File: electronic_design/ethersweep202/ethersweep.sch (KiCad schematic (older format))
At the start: 72 parts, among them J1 AVR-ISP-6, J2 Conn_01x02_Male, J3 Conn_01x04_Female, J4 Conn_01x02_Male, J5 Conn_01x02_Male, J6 HR911105A, J7 Conn_01x06_Female, J8 AVR-ISP-6, J9 Conn_01x06_Male, M1 Stepper_Motor_bipolar, SW1 SW_Push, U1 ENC28J60x-SS, U2 ATmega328-AU, U3 DRV8825PWPR, U4 AMS1117-3.3, U5 AS5600, Y1 Crystal_25MHz, Y3 Crystal

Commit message: minor v202 changes
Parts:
- added C?: C10uF, Capacitor_SMD:C_0805_2012Metric, symbol Device:C
- added C? (x6): C100nF, Capacitor_SMD:C_0805_2012Metric, symbol Device:C
- added C? (x2): C1uF, Capacitor_SMD:C_0805_2012Metric, symbol Device:C
- added J?: HR911105A, modules:HANRUN_HR911105A, symbol HR911105A:HR911105A
- added R?: R2M, symbol Device:R
- added R? (x2): R330, Resistor_SMD:R_0603_1608Metric, symbol Device:R
- added U?: W5500, Package_QFP:LQFP-48_7x7mm_P0.5mm, symbol Interface_Ethernet:W5500
- C4, C5: value C22pF -> C18pF
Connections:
- net +3V3: now also C?.1, C?.1, C?.1, C?.1, C?.1, C?.1, C?.1, C?.1, C?.1, J?.4, J?.5, U?.11 (AVDD), U?.15 (AVDD), U?.17 (AVDD), U?.21 (AVDD), U?.28 (VDD), U?.4 (AVDD), U?.8 (AVDD)
- net CS_ETHERNET: now also U?.32 (~SCS)
- net ENC_RD+: now also J?.3
- net ENC_RD-: now also J?.6
- net ENC_TD+: now also J?.1
- net ENC_TD-: now also J?.2
- net ETHERNET_LED_A: now also J?.12, R?.1
- net ETHERNET_LED_B: now also J?.9, R?.1
- net GND: now also C?.2, C?.2, C?.2, C?.2, C?.2, C?.2, C?.2, C?.2, C?.2, J?.10, J?.11, J?.15 (SHIELD), J?.16 (SHIELD), J?.8
- net MISO: now also U?.34 (MISO)
- net MOSI: now also U?.35 (MOSI)
- net SCK: now also U?.33 (SCLK)
- net at C4.2, U1.23 (OSC1), Y1.3: now also R?.1
- net at C5.1, U1.24 (OSC2), Y1.1: now also R?.2
- new net: U?.14 (AGND), U?.16 (AGND), U?.19 (AGND), U?.3 (AGND), U?.48 (AGND), U?.9 (AGND)
- new net: R?.2, U?.25 (LINKLED)
- new net: R?.2, U?.27 (ACTLED)
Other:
- moved on the sheet: C22, C23

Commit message: added photo
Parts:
- gave numbers to parts that had none: 14
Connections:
- net +12V: now also J2.2 (Pin_2); no longer J2.1 (Pin_1)
- net GND: now also J2.1 (Pin_1); no longer J2.2 (Pin_2)
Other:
- moved on the sheet: J2

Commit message: schematic changes
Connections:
- net +3V3: now also U3.17 (NSLEEP)
- net FLT_ETHERNET renamed FLT_STEPPER
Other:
- note added: "replace with buck converter"
- moved on the sheet: C20, C22, C23, J4, R1
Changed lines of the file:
@@
 L power:+3.3V #PWR0118
 U 1 1 605B1AAA
-P 9800 2900
-F 0 "#PWR0118" H 9800 2750 50  0001 C CNN
-F 1 "+3.3V" H 9815 3073 50  0000 C CNN
-F 2 "" H 9800 2900 50  0001 C CNN
-F 3 "" H 9800 2900 50  0001 C CNN
-	1    9800 2900
-	1    0    0    -1
-$EndComp
-Wire Wire Line
-	9800 3050 9800 2900
-Wire Wire Line
-	9800 3450 10100 3450
-Connection ~ 9800 3450
-Wire Wire Line
-	9700 3450 9800 3450
-Wire Wire Line
-	9800 3450 9800 3350
-Wire Wire Line
-	10100 3550 9950 3550
-Wire Wire Line
-	9950 3550 9950 3650
+P 9950 2900
+F 0 "#PWR0118" H 9950 2750 50  0001 C CNN
+F 1 "+3.3V" H 9965 3073 50  0000 C CNN
+F 2 "" H 9950 2900 50  0001 C CNN
+F 3 "" H 9950 2900 50  0001 C CNN
+	1    9950 2900
+	1    0    0    -1
+$EndComp
+Wire Wire Line
+	9950 3050 9950 2900
+Wire Wire Line
+	9950 3450 10250 3450
+Connection ~ 9950 3450
+Wire Wire Line
+	9850 3450 9950 3450
+Wire Wire Line
+	9950 3450 9950 3350
+Wire Wire Line
+	10250 3550 10100 3550
+Wire Wire Line
+	10100 3550 10100 3650
 $Comp
 L Device:R R1
 U 1 1 607B1186
-P 9800 3200
-F 0 "R1" H 9870 3246 50  0000 L CNN
-F 1 "R10k" H 9870 3155 50  0000 L CNN
-F 2 "Resistor_SMD:R_0603_1608Metric" V 9730 3200 50  0001 C CNN
-F 3 "~" H 9800 3200 50  0001 C CNN
-F 4 "C25804" H 9800 3200 50  0001 C CNN "LCSC"
-	1    9800 3200
+P 9950 3200
+F 0 "R1" H 10020 3246 50  0000 L CNN
+F 1 "R10k" H 10020 3155 50  0000 L CNN
+F 2 "Resistor_SMD:R_0603_1608Metric" V 9880 3200 50  0001 C CNN
+F 3 "~" H 9950 3200 50  0001 C CNN
+F 4 "C25804" H 9950 3200 50  0001 C CNN "LCSC"
+	1    9950 3200
 	1    0    0    -1
 $EndComp
@@
 L power:GND #PWR0107
 U 1 1 607B1180
-P 9950 3650
-F 0 "#PWR0107" H 9950 3400 50  0001 C CNN
-F 1 "GND" H 9955 3477 50  0000 C CNN
-F 2 "" H 9950 3650 50  0001 C CNN
-F 3 "" H 9950 3650 50  0001 C CNN
-	1    9950 3650
+P 10100 3650
+F 0 "#PWR0107" H 10100 3400 50  0001 C CNN
+F 1 "GND" H 10105 3477 50  0000 C CNN
+F 2 "" H 10100 3650 50  0001 C CNN
+F 3 "" H 10100 3650 50  0001 C CNN
+	1    10100 3650
 	1    0    0    -1
 $EndComp
@@
 L Connector:Conn_01x02_Male J4
 U 1 1 607B117A
-P 10300 3550
-F 0 "J4" H 10272 3432 50  0000 R CNN
-F 1 "Conn_01x02_Male" H 10272 3523 50  0000 R CNN
-F 2 "Connector_JST:JST_EH_S2B-EH_1x02_P2.50mm_Horizontal" H 10300 3550 50  0001 C CNN
-F 3 "~" H 10300 3550 50  0001 C CNN
-	1    10300 3550
+P 10450 3550
+F 0 "J4" H 10422 3432 50  0000 R CNN
+F 1 "Conn_01x02_Male" H 10422 3523 50  0000 R CNN
+F 2 "Connector_JST:JST_EH_S2B-EH_1x02_P2.50mm_Horizontal" H 10450 3550 50  0001 C CNN
+F 3 "~" H 10450 3550 50  0001 C CNN
+	1    10450 3550
 	-1   0    0    1
 $EndComp
-Text GLabel 9700 3450 0    50   Input ~ 0
+Text GLabel 9850 3450 0    50   Input ~ 0
 ESTOP
 $Comp
@@
 	12700 6700 12450 6700
 Text GLabel 14350 6300 2    50   Input ~ 0
-FLT_ETHERNET
+FLT_STEPPER
 $Comp
 L power:GND #PWR0159
@@
 L power:GND #PWR0167
 U 1 1 61514594
-P 14600 5450
-F 0 "#PWR0167" H 14600 5200 50  0001 C CNN
-F 1 "GND" H 14605 5277 50  0000 C CNN
-F 2 "" H 14600 5450 50  0001 C CNN
-F 3 "" H 14600 5450 50  0001 C CNN
-	1    14600 5450
-	1    0    0    -1
-$EndComp
-Wire Wire Line
-	14600 5400 14600 5450
+P 14500 7550
+F 0 "#PWR0167" H 14500 7300 50  0001 C CNN
+F 1 "GND" H 14505 7377 50  0000 C CNN
+F 2 "" H 14500 7550 50  0001 C CNN
+F 3 "" H 14500 7550 50  0001 C CNN
+	1    14500 7550
+	1    0    0    -1
+$EndComp
+Wire Wire Line
+	14500 7500 14500 7550
 $Comp
 L power:+12V #PWR0168
 U 1 1 6155B9EE
-P 14600 5050
-F 0 "#PWR0168" H 14600 4900 50  0001 C CNN
-F 1 "+12V" H 14615 5223 50  0000 C CNN
-F 2 "" H 14600 5050 50  0001 C CNN
-F 3 "" H 14600 5050 50  0001 C CNN
-	1    14600 5050
+P 14500 7150
+F 0 "#PWR0168" H 14500 7000 50  0001 C CNN
+F 1 "+12V" H 14515 7323 50  0000 C CNN
+F 2 "" H 14500 7150 50  0001 C CNN
+F 3 "" H 14500 7150 50  0001 C CNN
+	1    14500 7150
 	1    0    0    -1
 $EndComp
@@
 L power:GND #PWR0170
 U 1 1 615D9D8D
-P 15150 5500
-F 0 "#PWR0170" H 15150 5250 50  0001 C CNN
-F 1 "GND" H 15155 5327 50  0000 C CNN
-F 2 "" H 15150 5500 50  0001 C CNN
-F 3 "" H 15150 5500 50  0001 C CNN
-	1    15150 5500
-	1    0    0    -1
-$EndComp
-Wire Wire Line
-	15150 5450 15150 5500
+P 15000 7550
+F 0 "#PWR0170" H 15000 7300 50  0001 C CNN
+F 1 "GND" H 15005 7377 50  0000 C CNN
+F 2 "" H 15000 7550 50  0001 C CNN
+F 3 "" H 15000 7550 50  0001 C CNN
+	1    15000 7550
+	1    0    0    -1
+$EndComp
+Wire Wire Line
+	15000 7500 15000 7550
 $Comp
 L power:GND #PWR0172
 U 1 1 615F1838
-P 15500 5500
-F 0 "#PWR0172" H 15500 5250 50  0001 C CNN
-F 1 "GND" H 15505 5327 50  0000 C CNN
-F 2 "" H 15500 5500 50  0001 C CNN
-F 3 "" H 15500 5500 50  0001 C CNN
-	1    15500 5500
-	1    0    0    -1
-$EndComp
-Wire Wire Line
-	15500 5450 15500 5500
+P 15500 7550
+F 0 "#PWR0172" H 15500 7300 50  0001 C CNN
+F 1 "GND" H 15505 7377 50  0000 C CNN
+F 2 "" H 15500 7550 50  0001 C CNN
+F 3 "" H 15500 7550 50  0001 C CNN
+	1    15500 7550
+	1    0    0    -1
+$EndComp
+Wire Wire Line
+	15500 7500 15500 7550
 $Comp
 L power:+12V #PWR0171
 U 1 1 615F1832
-P 15500 5100
-F 0 "#PWR0171" H 15500 4950 50  0001 C CNN
-F 1 "+12V" H 15515 5273 50  0000 C CNN
-F 2 "" H 15500 5100 50  0001 C CNN
-F 3 "" H 15500 5100 50  0001 C CNN
-	1    15500 5100
-	1    0    0    -1
-$EndComp
-Wire Wire Line
-	15500 5100 15500 5150
+P 15500 7150
+F 0 "#PWR0171" H 15500 7000 50  0001 C CNN
+F 1 "+12V" H 15515 7323 50  0000 C CNN
+F 2 "" H 15500 7150 50  0001 C CNN
+F 3 "" H 15500 7150 50  0001 C CNN
+	1    15500 7150
+	1    0    0    -1
+$EndComp
+Wire Wire Line
+	15500 7150 15500 7200
 $Comp
 L Device:C C23
 U 1 1 615F182B
-P 15500 5300
-F 0 "C23" H 15615 5346 50  0000 L CNN
-F 1 "C100nF" H 15615 5255 50  0000 L CNN
-F 2 "Capacitor_SMD:C_0805_2012Metric" H 15538 5150 50  0001 C CNN
-F 3 "~" H 15500 5300 50  0001 C CNN
-F 4 "C49678" H 15500 5300 50  0001 C CNN "LCSC"
-	1    15500 5300
+P 15500 7350
+F 0 "C23" H 15615 7396 50  0000 L CNN
+F 1 "C100nF" H 15615 7305 50  0000 L CNN
+F 2 "Capacitor_SMD:C_0805_2012Metric" H 15538 7200 50  0001 C CNN
+F 3 "~" H 15500 7350 50  0001 C CNN
+F 4 "C49678" H 15500 7350 50  0001 C CNN "LCSC"
+	1    15500 7350
 	1    0    0    -1
 $EndComp
@@
 L power:+12V #PWR0169
 U 1 1 615C30C1
-P 15150 5100
-F 0 "#PWR0169" H 15150 4950 50  0001 C CNN
-F 1 "+12V" H 15165 5273 50  0000 C CNN
-F 2 "" H 15150 5100 50  0001 C CNN
-F 3 "" H 15150 5100 50  0001 C CNN
-	1    15150 5100
-	1    0    0    -1
-$EndComp
-Wire Wire Line
-	15150 5100 15150 5150
+P 15000 7150
+F 0 "#PWR0169" H 15000 7000 50  0001 C CNN
+F 1 "+12V" H 15015 7323 50  0000 C CNN
+F 2 "" H 15000 7150 50  0001 C CNN
+F 3 "" H 15000 7150 50  0001 C CNN
+	1    15000 7150
+	1    0    0    -1
+$EndComp
+Wire Wire Line
+	15000 7150 15000 7200
 $Comp
 L Device:C C22
 U 1 1 615AC4BC
-P 15150 5300
-F 0 "C22" H 15265 5346 50  0000 L CNN
-F 1 "C100nF" H 15265 5255 50  0000 L CNN
-F 2 "Capacitor_SMD:C_0805_2012Metric" H 15188 5150 50  0001 C CNN
-F 3 "~" H 15150 5300 50  0001 C CNN
-F 4 "C49678" H 15150 5300 50  0001 C CNN "LCSC"
-	1    15150 5300
-	1    0    0    -1
-$EndComp
-Wire Wire Line
-	14600 5050 14600 5100
+P 15000 7350
+F 0 "C22" H 15115 7396 50  0000 L CNN
+F 1 "C100nF" H 15115 7305 50  0000 L CNN
+F 2 "Capacitor_SMD:C_0805_2012Metric" H 15038 7200 50  0001 C CNN
+F 3 "~" H 15000 7350 50  0001 C CNN
+F 4 "C49678" H 15000 7350 50  0001 C CNN "LCSC"
+	1    15000 7350
+	1    0    0    -1
+$EndComp
+Wire Wire Line
+	14500 7150 14500 7200
 $Comp
 L Device:CP1 C20
 U 1 1 6151458E
-P 14600 5250
-F 0 "C20" H 14715 5296 50  0000 L CNN
-F 1 "C100uF" H 14715 5205 50  0000 L CNN
-F 2 "Capacitor_SMD:CP_Elec_8x10" H 14600 5250 50  0001 C CNN
-F 3 "~" H 14600 5250 50  0001 C CNN
-F 4 "C176665" H 14600 5250 50  0001 C CNN "LCSC"
-	1    14600 5250
+P 14500 7350
+F 0 "C20" H 14615 7396 50  0000 L CNN
+F 1 "C100uF" H 14615 7305 50  0000 L CNN
+F 2 "Capacitor_SMD:CP_Elec_8x10" H 14500 7350 50  0001 C CNN
+F 3 "~" H 14500 7350 50  0001 C CNN
+F 4 "C176665" H 14500 7350 50  0001 C CNN "LCSC"
+	1    14500 7350
 	1    0    0    -1
 $EndComp
@@
 Wire Wire Line
 	2050 2500 2300 2500
-Text GLabel 2300 2800 2    50   Input ~ 0
-FLT_ETHERNET
 Wire Wire Line
 	2050 2800 2300 2800
@@
 	0    -1   -1   0
 $EndComp
+Wire Wire Line
+	12700 6800 12550 6800
+$Comp
+L power:+3.3V #PWR?
+U 1 1 60CB2D51
+P 12550 6800
+F 0 "#PWR?" H 12550 6650 50  0001 C CNN
+F 1 "+3.3V" H 12565 6973 50  0000 C CNN
+F 2 "" H 12550 6800 50  0001 C CNN
+F 3 "" H 12550 6800 50  0001 C CNN
+	1    12550 6800
+	0    -1   -1   0
+$EndComp
+Text GLabel 2300 2800 2    50   Input ~ 0
+FLT_STEPPER
+Text Notes 12850 2150 0    50   ~ 0
+replace with buck converter
 $EndSCHEMATC

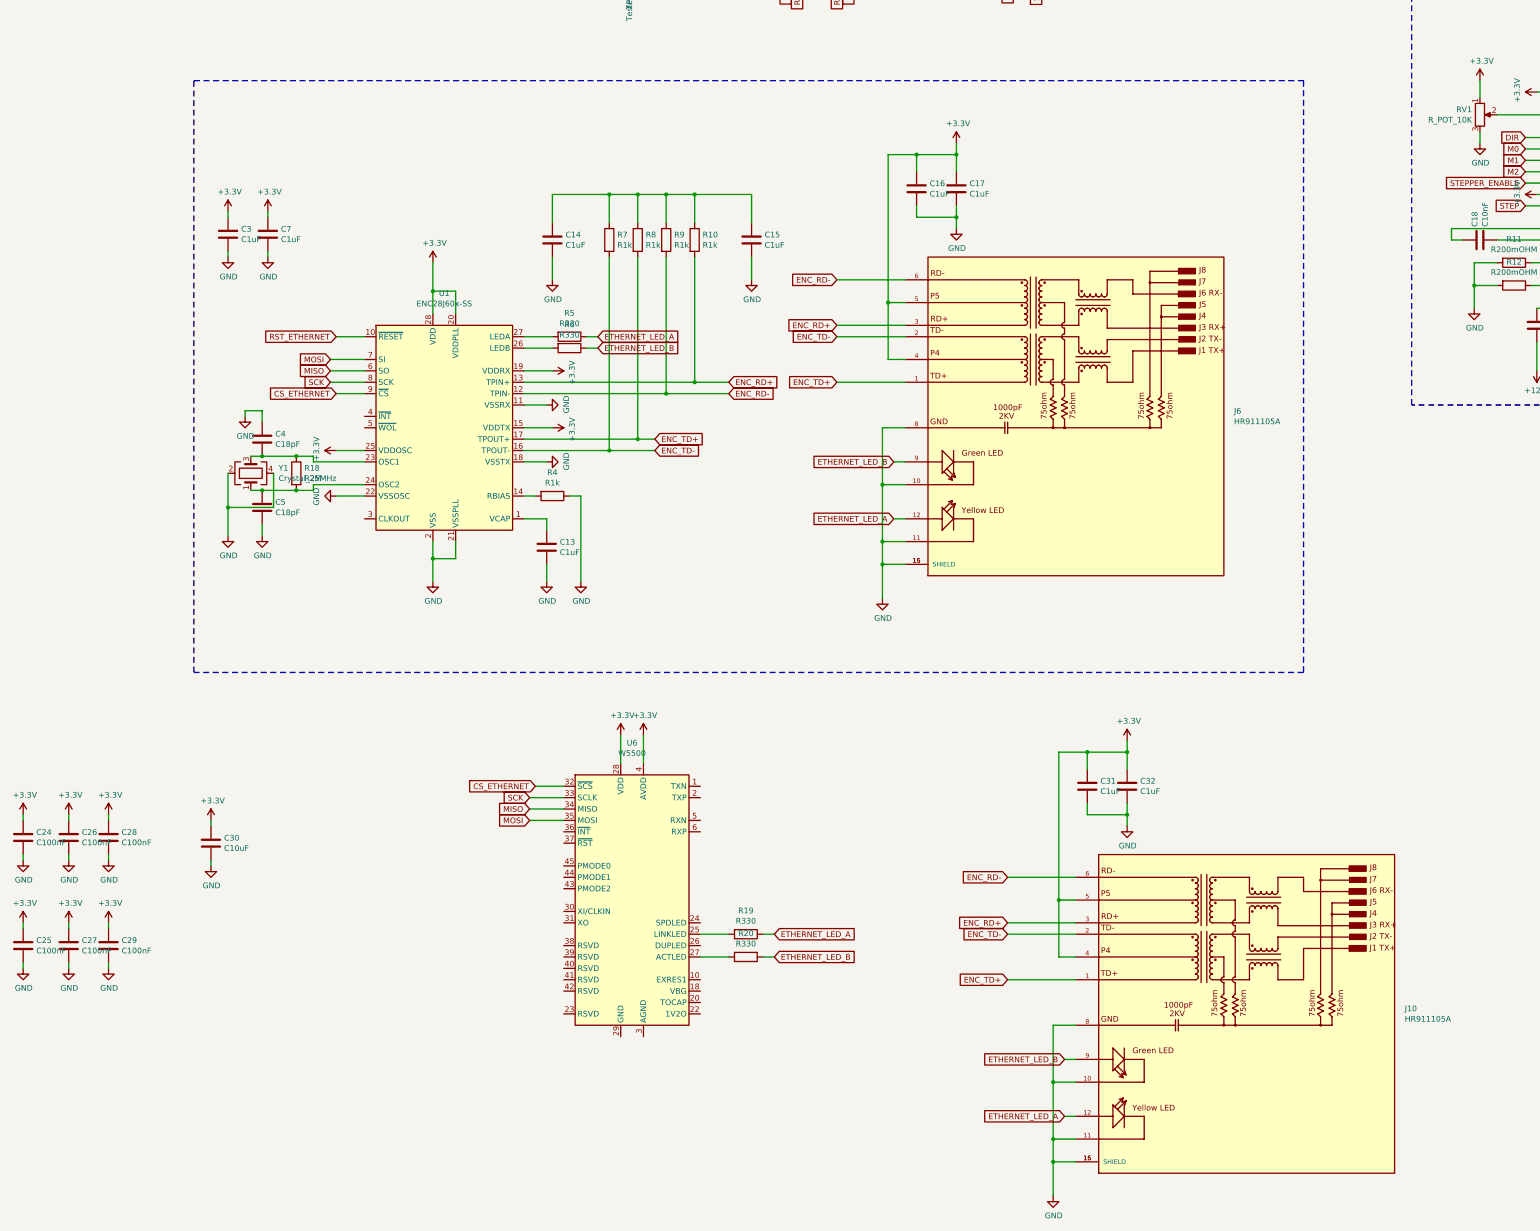
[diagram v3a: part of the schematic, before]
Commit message: 202 design changed to w5500 ethernet driver
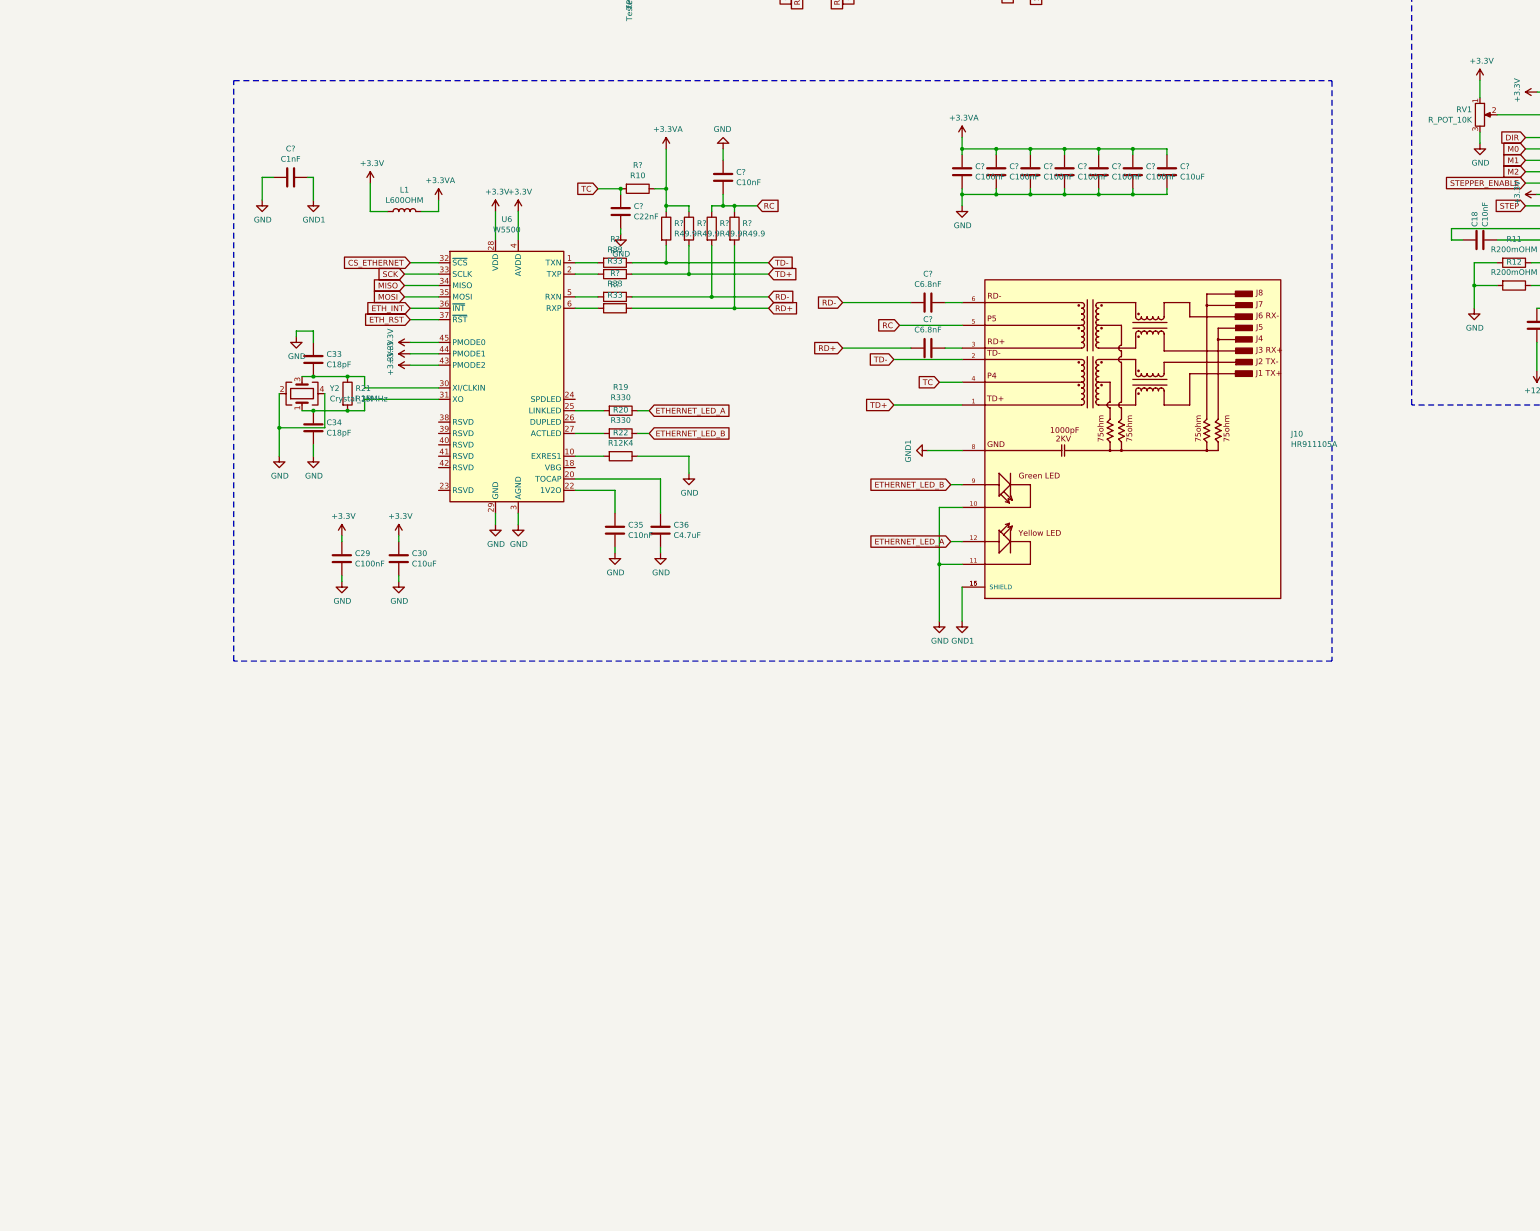
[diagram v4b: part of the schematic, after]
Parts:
- removed C13, C14, C15, C16, C17, C3, C31, C32, C7: C1uF, Capacitor_SMD:C_0805_2012Metric, symbol Device:C
- removed C24, C25, C26, C27, C28: C100nF, Capacitor_SMD:C_0805_2012Metric, symbol Device:C
- removed C4, C5: C18pF, Capacitor_SMD:C_0402_1005Metric, symbol Device:C
- removed J6: HR911105A, modules:HANRUN_HR911105A, symbol HR911105A:HR911105A
- removed R10, R4, R7, R8, R9: R1k, Resistor_SMD:R_0603_1608Metric, symbol Device:R
- removed R18: R2M, symbol Device:R
- removed R5, R6: R330, Resistor_SMD:R_0603_1608Metric, symbol Device:R
- removed U1: ENC28J60x-SS, Package_SO:SSOP-28_5.3x10.2mm_P0.65mm, symbol Interface_Ethernet:ENC28J60x-SS
- removed Y1: Crystal_25MHz, Crystal:Crystal_SMD_3225-4Pin_3.2x2.5mm, symbol Device:Crystal_GND24
- added C33, C34: C18pF, Capacitor_SMD:C_0402_1005Metric, symbol Device:C
- added C35, C?: C10nF, Capacitor_SMD:C_0603_1608Metric, symbol Device:C
- added C36: C4.7uF, Capacitor_SMD:C_0402_1005Metric, symbol Device:C
- added C?: C1nF, Resistor_SMD:R_1206_3216Metric, symbol Device:C
- added C? (x2): C6.8nF, Resistor_SMD:R_0402_1005Metric, symbol Device:C
- added C?: C22nF, Resistor_SMD:R_0603_1608Metric, symbol Device:C
- added C? (x6): C100nF, Capacitor_SMD:C_0402_1005Metric, symbol Device:C
- added C?: C10uF, Capacitor_SMD:C_0805_2012Metric, symbol Device:C
- added L1: L600OHM, symbol Device:L
- added R21: R1M, Resistor_SMD:R_0805_2012Metric, symbol Device:R
- added R22: R12K4, Resistor_SMD:R_0805_2012Metric, symbol Device:R
- added R? (x4): R33, Resistor_SMD:R_0805_2012Metric, symbol Device:R
- added R? (x4): R49.9, Resistor_SMD:R_0603_1608Metric, symbol Device:R
- added R?: R10, Resistor_SMD:R_0805_2012Metric, symbol Device:R
- added Y2: Crystal_25MHz, Crystal:Crystal_SMD_3225-4Pin_3.2x2.5mm, symbol Device:Crystal_GND24
- C29: footprint Capacitor_SMD:C_0805_2012Metric -> Capacitor_SMD:C_0402_1005Metric; LCSC C49678 -> C1525
- C30: LCSC (none) -> C15850
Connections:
- net +3V3: now also U6.43 (PMODE2), U6.44 (PMODE1), U6.45 (PMODE0), L1.1; no longer J10.4, J10.5
- net GND: now also U6.14 (AGND), U6.16 (AGND), U6.19 (AGND), U6.29 (GND), U6.3 (AGND), U6.48 (AGND), U6.9 (AGND), C33.1, C34.2, C35.2, C36.2, C?.1, C?.1, C?.2, C?.2, C?.2, C?.2, C?.2, C?.2, C?.2, C?.2, R22.1, Y2.2, Y2.4; no longer J10.15 (SHIELD), J10.16 (SHIELD), J10.8
- net at U6.1 (TXN): now also R?.2
- net at U6.10 (EXRES1): now also R22.2
- net at U6.2 (TXP): now also R?.2
- net at U6.20 (TOCAP): now also C36.1
- net at U6.22 (1V2O): now also C35.1
- net at U6.30 (XI/CLKIN): now also C33.2, R21.1, Y2.3
- net at U6.31 (XO): now also C34.1, R21.2, Y2.1
- net ETH_INT: now reaches U6.36 (~INT)
- net ETH_RST: now reaches U6.37 (~RST)
- net at U6.5 (RXN): now also R?.2
- net at U6.6 (RXP): now also R?.2
- net ENC_RD+: no longer names the net of J10.3
- net ENC_RD+: now also C?.1
- net ENC_RD-: no longer names the net of J10.6
- net ENC_RD-: now also C?.1
- net ENC_TD+ renamed TD+
- net TD+: now also R?.1, R?.2
- net ENC_TD- renamed TD-
- net TD-: now also R?.1, R?.2
- new net +3.3VA: C?.1, C?.1, C?.1, C?.1, C?.1, C?.1, C?.1, L1.2, R?.1, R?.1, R?.1
- new net GND1: C?.1, J10.15 (SHIELD), J10.16 (SHIELD), J10.8
- new net RC: C?.2, J10.5, R?.1, R?.1
- new net RD+: C?.2, R?.1, R?.2
- new net RD-: C?.2, R?.1, R?.2
- new net TC: C?.2, J10.4, R?.2
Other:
- moved on the sheet: C29, C30, J10, R19, R20, U6

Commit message: cleanup
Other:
- note added: "OLED"
- note added: "PCB Bridge"
- moved on the sheet: C1, C10, C8, H1, H2, H3, H4, H5, H6, H7, H8, J1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
